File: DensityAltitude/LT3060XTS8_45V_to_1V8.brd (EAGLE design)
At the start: 63.5 x 57.1 mm, 15 parts, among them U1 V_REG_LD1086V

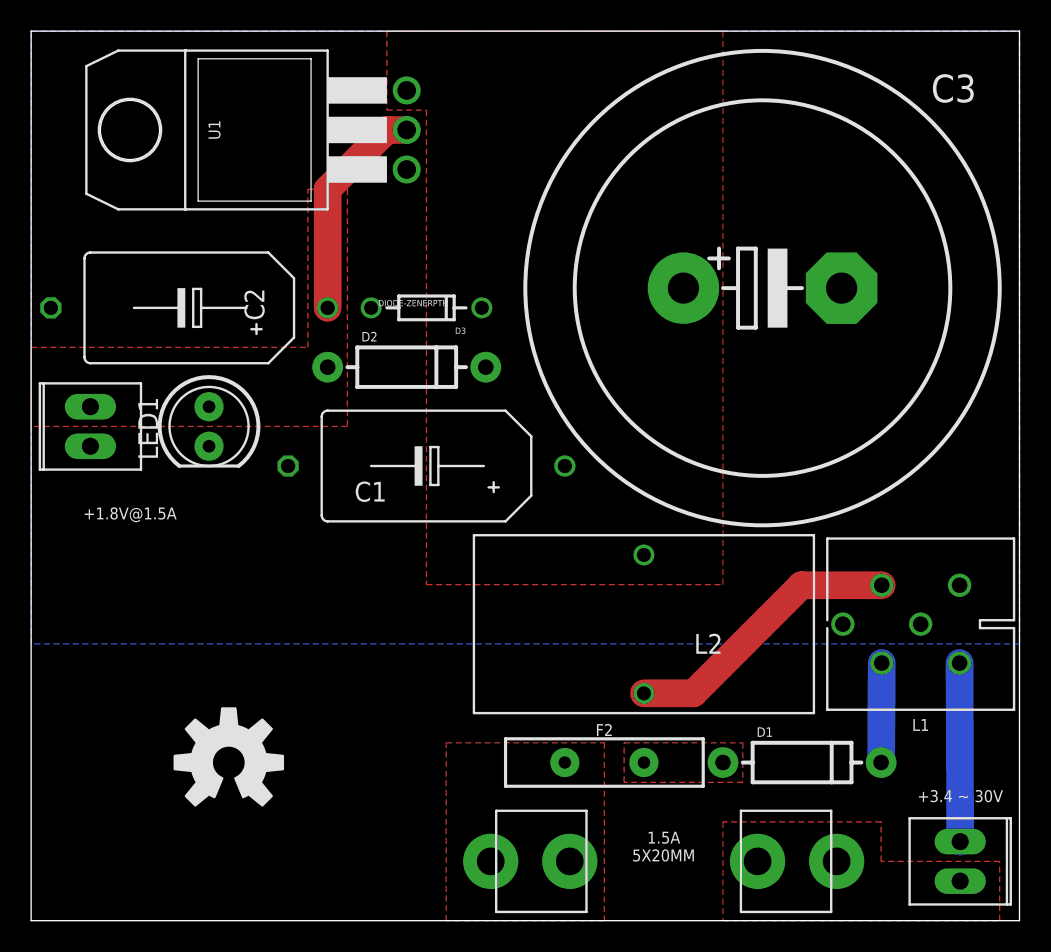
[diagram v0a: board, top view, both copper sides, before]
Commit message: Moved 1V8 voltage regulators from DensityAltitude.lbr to 1V8.lbr More layout work for various high input voltage regulators A bit more work on LowduinoPTH_v2
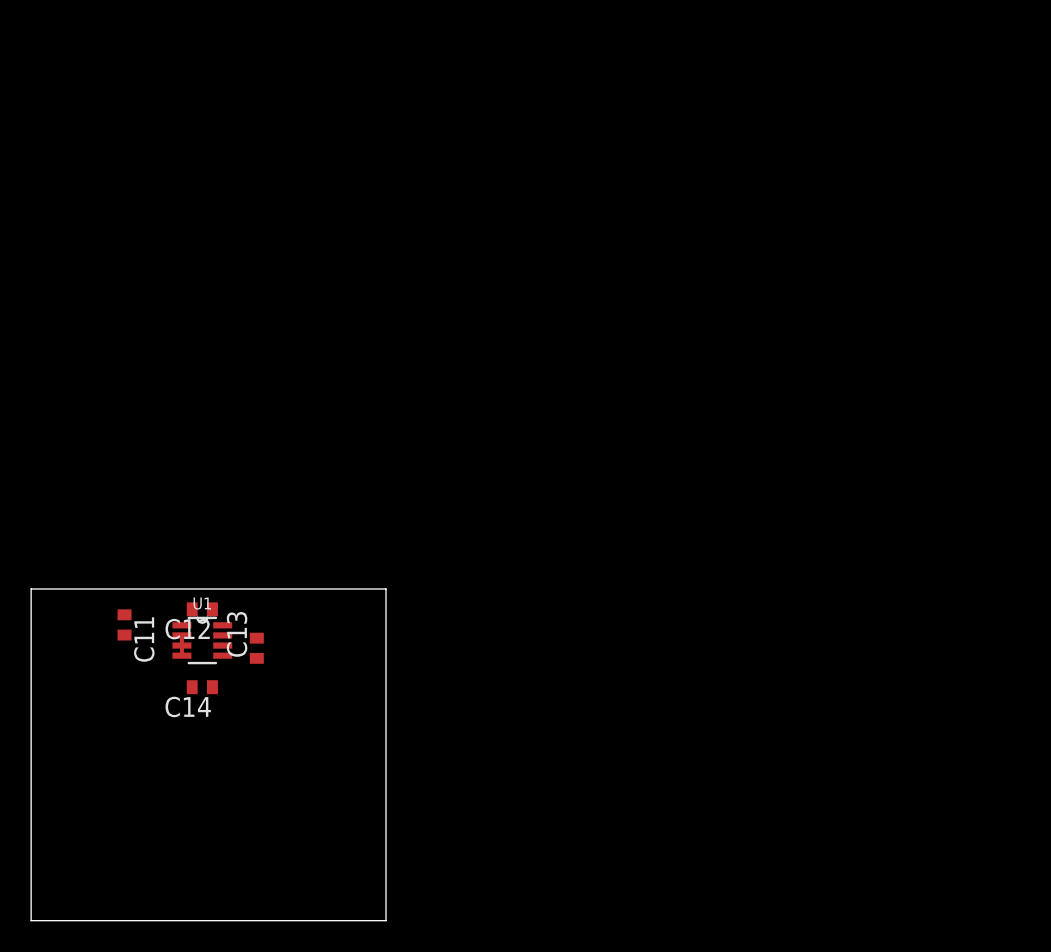
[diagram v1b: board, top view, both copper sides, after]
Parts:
- removed C1, C2: 10uF, 1V8:KEMET_E
- removed C3: (no value), rcl:EB30D
- removed D1, D2: (no value), SparkFun-DiscreteSemi:DIODE-1N4001
- removed D3: DIODE-ZENERPTH, SparkFun-DiscreteSemi:DIODE-ZENER
- removed F1: FUSE5X20MM, DensityAltitude:FUSE_1A3399
- removed F2: PTCPTH, DensityAltitude:PTC
- removed JP1, JP2: (no value), DensityAltitude:1X02_282834-2
- removed L1: BNX002, 1V8:BNX002
- removed L2: 2121-RC-VERT, DensityAltitude:2121-RC-VERT
- removed LED1: (no value), SparkFun-LED:LED5MM
- removed U$2: (no value), SparkFun-Aesthetics:OSHW-LOGO-L
- added C11: 1uF, rcl:C0402
- added C12, C13: 10nF, rcl:C0402
- added C14: 10uF, rcl:C0402
- U1: value V_REG_LD1086V -> LT3060ETS8; device DensityAltitude:TO-220-SINGLE -> 1V8:LINEAR_TS8
- moved U1 33.1 mm to (11.0, 18.0), turned to 0 degrees
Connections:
- removed net DIODE1: D1.C, L1.B
- removed net FILTERED: C1.+, C3.+, D2.C, D3.P$1, L2.2, U1.IN
- removed net FUSE1: F1.3, F1.4, F2.P$1
- removed net FUSE2: D1.A, F2.P$2
- removed net GND-ISO: C1.-, C2.-, C3.-, D3.P$2, JP2.P$1, L1.CG, L1.CG1, L1.CG2, LED1.K, U1.GND
- removed net N$1: L1.CB, L2.1
- removed net VCC: C2.+, D2.A, JP2.P$2, LED1.A, U1.OUT
- new net N$2: C13.2, U1.7
- new net N$5: C12.1, U1.8
- new net OUT: C13.1, C14.1, U1.6
- net GND: now also C11.2, C12.2, C14.2, U1.2, U1.3, U1.4; no longer JP1.P$1, L1.PSG
- net VIN: now also C11.1, U1.1, U1.5; no longer F1.1, F1.2, JP1.P$2
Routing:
- net N$1: track 18.2 -> 0.00 mm
- net VCC: track 14.3 -> 0.00 mm
- net GND: track 11.5 -> 1.30 mm
- net DIODE1: track 6.39 -> 0.00 mm
- removed copper zone on layer 1, net FILTERED
- removed copper zone on layer 1, net FUSE1
- removed copper zone on layer 1, net FUSE2
- removed copper zone on layer 16, net GND-ISO
- removed copper zone on layer 1, net VCC
- removed copper zone on layer 1, net VIN
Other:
- board size 63.5 x 57.1 mm -> 22.8 x 21.3 mm
- board text removed: "+1.8V@1.5A"
- board text removed: "+3.4 ~ 30V"
- board text removed: "1.5A 5X20MM"
